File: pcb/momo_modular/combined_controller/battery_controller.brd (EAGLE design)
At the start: 31.8 x 33 mm, 39 parts, among them Q1 P-MOSFET, Q2 P-MOSFET, U1 XRP7659, U2 MAX1555, U3 MCP1702, U4 PIC24F16KA101-X_PSSOP, U5 FLASH8MSOP8

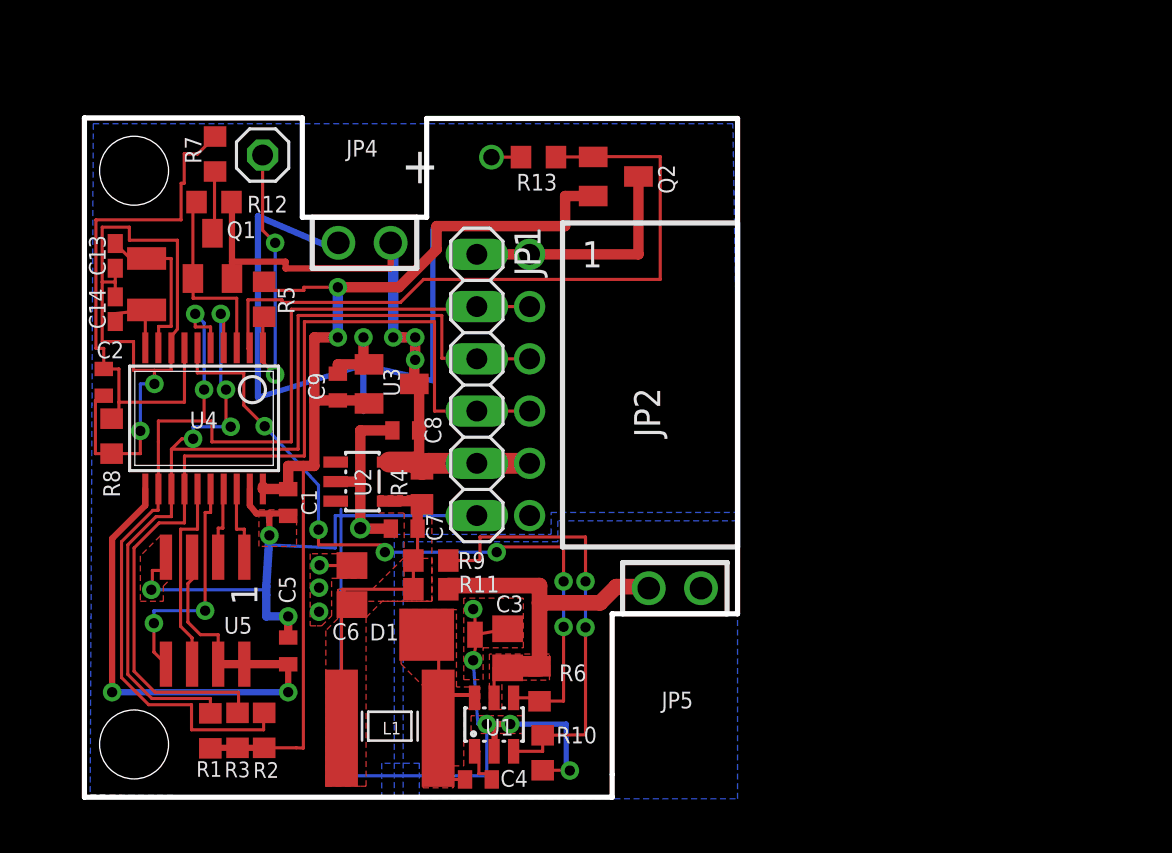
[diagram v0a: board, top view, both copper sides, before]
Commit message: Revised combined controller board into what should be the final version.  Added a current sense circuit to track battery charging, relaid traces out and swapped out the charger IC for a much cheaper one with a disable signal.
Added a schottky diode on the input in all assembly variants to prevent reverse polarity charging and to prevent discharging into the charger if the charger loses power.
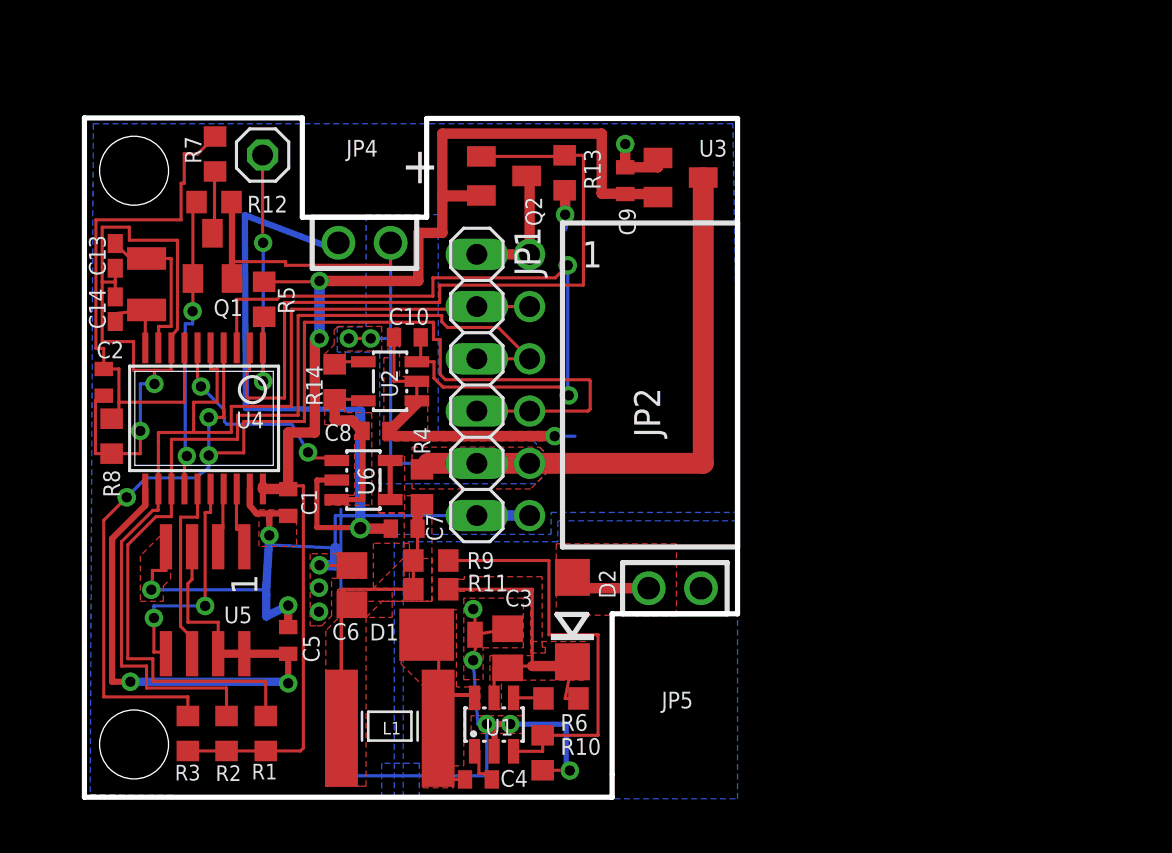
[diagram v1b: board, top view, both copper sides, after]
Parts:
- added C10: 100 nF, rcl:C0402
- added D2: (no value), diode:DO214AC
- added R14: (no value), rcl:R0603
- added U6: MCP73811, components:SOT23-5L
- U2: value MAX1555 -> MAX9938; device maxim:SOT23-5L -> components:SOT23-5L
- moved U3 17.3 mm to (63.1, 42.2)
- moved C9 17.2 mm to (60.5, 42.0)
- moved Q2 5.44 mm to (54.6, 42.3)
- moved U2 5.06 mm to (49.0, 32.3), turned to 90 degrees
- moved R1 2.70 mm to (43.0, 15.2)
- moved R3 2.42 mm to (39.2, 15.2)
- moved R2 1.84 mm to (41.1, 15.2)
- moved R13 1.48 mm to (57.5, 42.4), turned to 90 degrees
- moved C8 1.45 mm to (48.3, 29.9), turned to 0 degrees
- moved R6 1.26 mm to (57.3, 16.9), turned to 0 degrees
- moved C5 0.51 mm to (44.1, 19.7)
- moved U5 0.51 mm to (40.0, 21.6)
- renumbered XTAL1 to XT1
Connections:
- new net CHG_CURR: C10.1, U2.3, U4.3
- new net CHG_EN: U4.6, U6.1
- new net N$1: C3.1, D2.C, R11.1, R6.2, U1.5
- new net N$4: C8.1, R14.1, U2.5, U6.3
- net +18V: now also D2.A; no longer C3.1, R11.1, R6.2, U1.5
- net BUCK_EN: no longer U4.6
- net GND: now also C10.2, U2.1, U6.2
- net IDAT: no longer U4.4
- net IRQ: now also U4.4; no longer U4.14
- net N$5: now also U6.4, U6.5; no longer U2.4
- net SAMP_EN: now also U4.14; no longer U4.3
- net V+: now also R14.2, U2.4; no longer C8.1, U2.5
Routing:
- net CHG_CURR: track 0.00 -> 36.1 mm, vias 0 -> 2
- net BUCK_EN: track 35.9 -> 1.68 mm, vias 6 -> 0
- net V+: track 33.8 -> 58.7 mm, vias 3 -> 2
- net N$1: track 0.00 -> 16.2 mm
- net IRQ: track 46.4 -> 61.1 mm, vias 0 -> 3
- net +18V: track 18.4 -> 4.70 mm
- net VCCINT: track 54.6 -> 65.8 mm
- net GND: track 155.3 -> 166.3 mm, vias 16 -> 17
- net CHG_EN: track 0.00 -> 10.8 mm, vias 0 -> 2
- net N$4: track 0.00 -> 8.71 mm
- net ICLK: track 56.6 -> 49.8 mm, vias 2 -> 0
- net IDAT: track 54.9 -> 48.5 mm, vias 4 -> 0
- net SAMP_EN: track 9.29 -> 14.8 mm, vias 0 -> 2
- net VCCIO: track 11.6 -> 6.52 mm
- net VCC_EN: track 34.2 -> 35.6 mm
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- added copper zone on layer 1, net N$1
- added copper zone on layer 1, net N$4
- added copper zone on layer 1, net V+
- added copper zone on layer 16, net V+

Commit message: Moved pcb parts around on the controller to facilitate assembly.
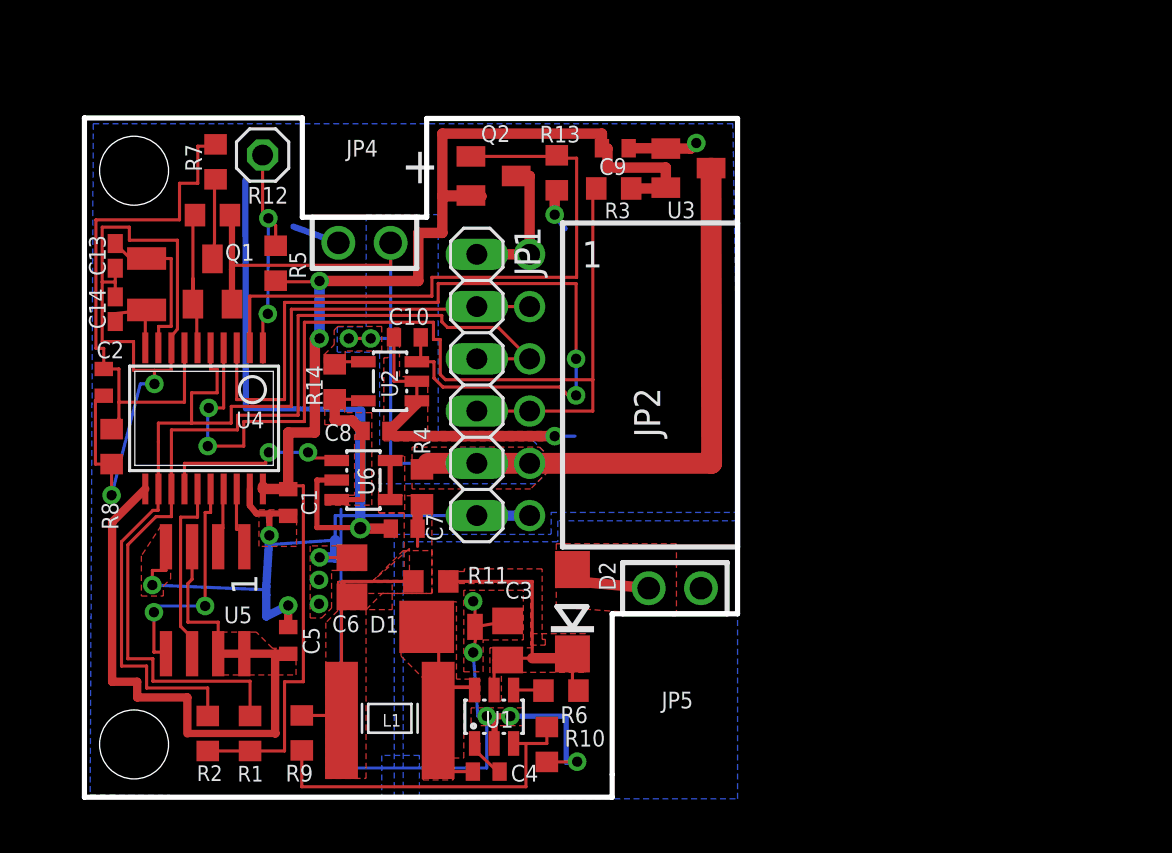
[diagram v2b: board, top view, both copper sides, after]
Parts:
- moved R3 33.6 mm to (59.9, 41.7), turned to 0 degrees
- moved R9 10.5 mm to (44.7, 15.2), turned to 90 degrees
- moved R5 1.84 mm to (43.5, 38.0), turned to 270 degrees
- moved C9 1.65 mm to (60.0, 43.6), turned to 0 degrees
- moved Q1 1.24 mm to (40.4, 37.1)
- moved R2 0.91 mm to (40.2, 15.2)
- moved R1 0.76 mm to (42.2, 15.2)
- moved R12 0.64 mm to (40.4, 40.4)
- moved U3 0.60 mm to (63.5, 42.6)
- moved C4 0.54 mm to (53.7, 13.3)
- moved R8 0.51 mm to (35.5, 29.1)
- moved Q2 0.51 mm to (54.1, 42.3)
- moved R10 0.45 mm to (56.6, 14.6)
- moved R7 0.38 mm to (40.5, 43.0)
- moved C3 0.38 mm to (54.7, 19.7)
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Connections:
- net CHG_EN: now also U4.14; no longer U4.6
- net SAMP_EN: now also U4.6; no longer U4.14
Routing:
- net IRQ: track 61.1 -> 49.6 mm, vias 3 -> 2
- net SAMP_EN: track 14.8 -> 8.85 mm, vias 2 -> 0
- net CHG_CURR: track 36.1 -> 40.5 mm
- net MEM_POW: track 30.3 -> 34.6 mm, vias 2 -> 0
- net VCC_EN: track 35.6 -> 31.7 mm
- net N$10: track 20.7 -> 17.2 mm
- net N$15: track 14.2 -> 11.8 mm
- net V+: track 58.7 -> 60.2 mm
- net GND: track 166.3 -> 167.7 mm
- net ICLK: track 49.8 -> 48.5 mm
- net CHG_EN: track 10.8 -> 9.50 mm
- net IDAT: track 48.5 -> 47.8 mm
- net N$3: track 3.89 -> 4.59 mm
- net VCCIO: track 6.52 -> 7.03 mm
- added copper zone on layer 1, net MEM_POW

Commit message: Added ability to specify FOOTPRINTS and DESCRIPTIONS using Eagle attributes and have the production scripts pick those up and use them in producing BOM descriptions and footprints.
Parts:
- L1: value 4.7 uF -> 4.7 uH
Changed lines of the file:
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@@
 <attribute name="DIGIKEY-PN-EXTPOWER" value="P100KHCT-ND" x="57.3278" y="17.2466" size="1.778" layer="27" display="off"/>
 </element>
-<element name="L1" library="components" package="NR6028-INDUCTOR" value="4.7 uF" x="51.3588" y="15.7988" smashed="yes" rot="R180">
+<element name="L1" library="components" package="NR6028-INDUCTOR" value="4.7 uH" x="51.3588" y="15.7988" smashed="yes" rot="R180">
 <attribute name="NAME" x="48.651" y="15.499" size="0.6096" layer="21"/>
 <attribute name="DIGIKEY-PN-BATT" value="587-2100-1-ND" x="51.3588" y="15.7988" size="1.778" layer="27" rot="R180" display="off"/>

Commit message: Remove unnecessary transistor and current sense
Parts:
- removed C10: 100 nF, rcl:C0402
- removed Q1: P-MOSFET, components:SOT23
- removed R12: 100K, rcl:R0603
- removed R14: (no value), rcl:R0603
- removed U2: MAX9938, components:SOT23-5L
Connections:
- removed net CHG_CURR: C10.1, U2.3, U4.3
- removed net N$3: Q1.3, R7.2
- removed net N$4: C8.1, R14.1, U2.5, U6.3
- removed net SAMP_EN: Q1.1, R12.2, U4.6
- net GND: no longer C10.2, U2.1, U2.2
- net V+: now also C8.1, R7.2, U6.3; no longer Q1.2, R12.1, R14.2, U2.4
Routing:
- net CHG_CURR: track 40.5 -> 0.00 mm, vias 2 -> 0
- net V+: track 60.2 -> 50.0 mm
- net SAMP_EN: track 8.85 -> 0.00 mm
- net N$4: track 8.71 -> 0.00 mm
- net GND: track 167.7 -> 161.5 mm
- net N$3: track 4.59 -> 0.00 mm
- removed copper zone on layer 1, net N$4

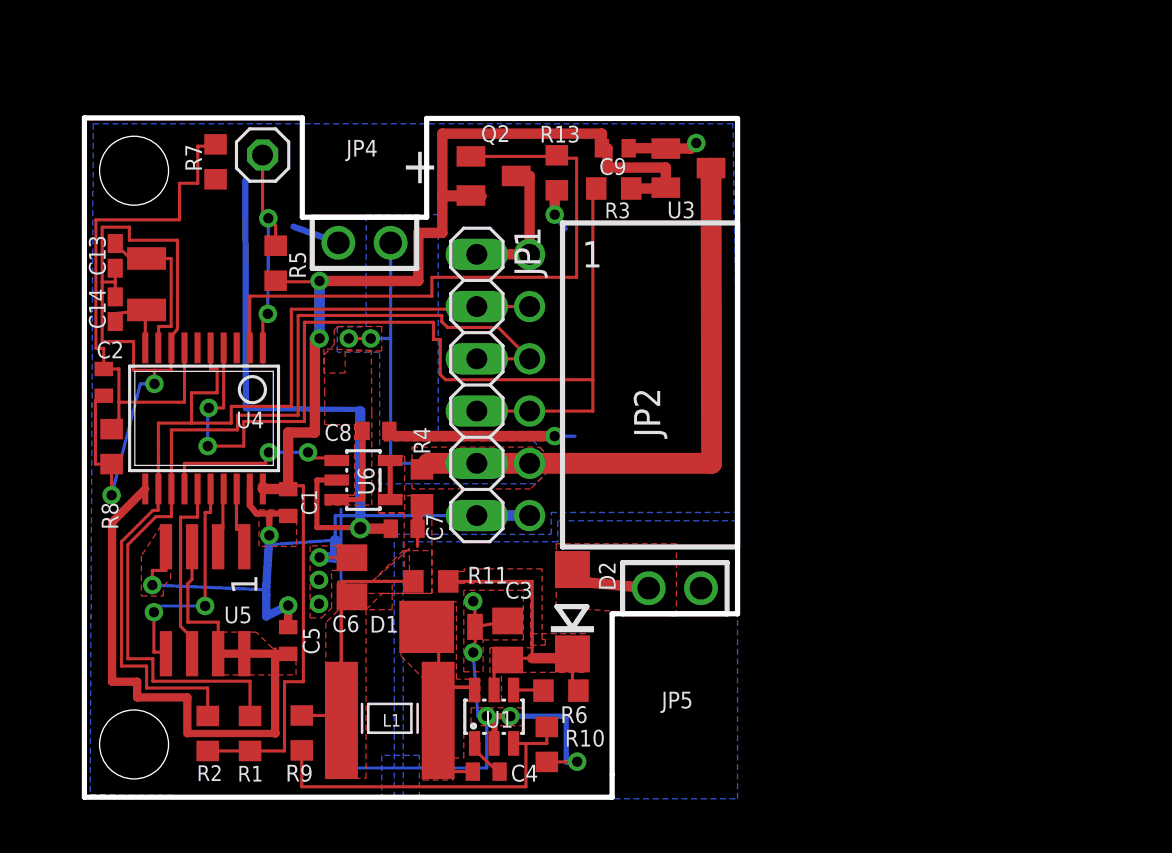
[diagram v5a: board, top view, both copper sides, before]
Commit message: Re-layout the controller board for 1M form factor
Not done but mostly there.
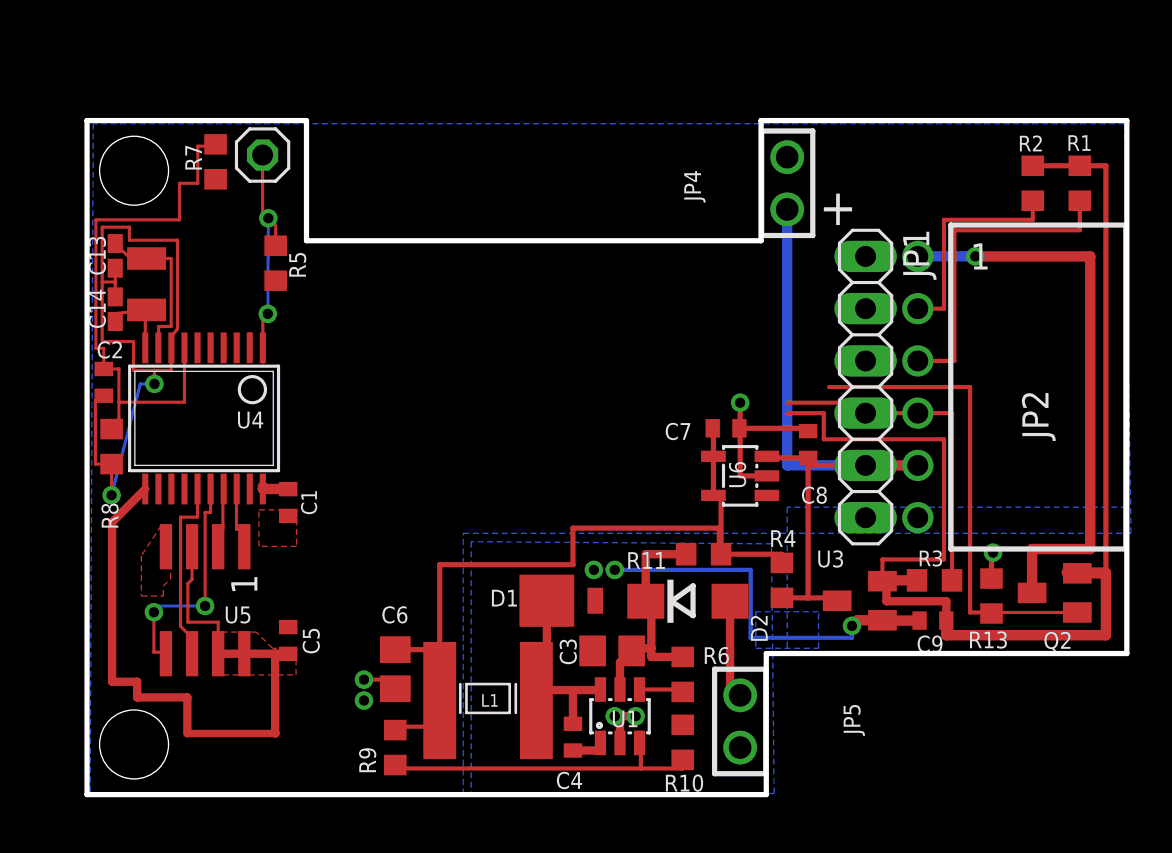
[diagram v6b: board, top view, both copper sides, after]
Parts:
- moved R1 48.4 mm to (82.5, 41.9), turned to 90 degrees
- moved R2 48.2 mm to (80.3, 41.9), turned to 90 degrees
- moved Q2 34.0 mm to (81.3, 22.0), turned to 90 degrees
- moved R13 29.5 mm to (78.3, 21.8), turned to 270 degrees
- moved C9 27.7 mm to (75.4, 20.7), turned to 180 degrees
- moved R3 24.6 mm to (75.5, 22.6), turned to 180 degrees
- moved U3 22.6 mm to (71.9, 21.6), turned to 90 degrees
- moved C8 21.0 mm to (69.3, 29.2), turned to 90 degrees
- moved JP4 20.8 mm to (68.3, 41.9), turned to 90 degrees
- moved JP1 18.9 mm to (72.1, 29.5)
- moved JP2 18.9 mm to (74.7, 28.2)
- moved U6 18.3 mm to (66.0, 27.7), turned to 90 degrees
- moved R4 18.1 mm to (68.1, 22.6), turned to 270 degrees
- moved C7 16.4 mm to (65.4, 30.0), turned to 0 degrees
- moved R11 13.3 mm to (64.3, 23.9), turned to 0 degrees
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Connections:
- net +18V: now also JP5.2; no longer JP5.1
- net GND: now also JP4.1, JP5.1; no longer JP4.2, JP5.2
- net V+: now also JP4.2; no longer JP4.1
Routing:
- net GND: track 161.5 -> 68.7 mm, vias 17 -> 11
- net ICLK: track 48.5 -> 10.8 mm
- net IRQ: track 49.6 -> 16.6 mm, vias 2 -> 0
- net IDAT: track 47.8 -> 15.7 mm
- net N$5: track 17.4 -> 41.3 mm
- net VCCIO: track 7.03 -> 27.6 mm, vias 0 -> 1
- net V+: track 50.0 -> 33.3 mm, vias 2 -> 0
- net CHG_EN: track 9.50 -> 0.00 mm, vias 2 -> 0
- net VCC_EN: track 31.7 -> 24.1 mm
- net N$1: track 15.8 -> 11.9 mm
- net N$13: track 13.1 -> 9.32 mm
- net N$10: track 17.2 -> 15.9 mm
- net BUCK_EN: track 1.68 -> 2.22 mm
- net VCCINT: track 65.7 -> 65.6 mm, vias 2 -> 0
- removed copper zone on layer 1, net +18V
- removed copper zone on layer 1, net N$1
- removed copper zone on layer 1, net N$13
- removed copper zone on layer 1, net N$5
- removed copper zone on layer 1, net V+
- removed copper zone on layer 16, net V+
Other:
- board size 31.8 x 33 mm -> 50.5 x 32.8 mm
